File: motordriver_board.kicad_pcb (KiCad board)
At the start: 2 copper layers, 99.9 x 99.9 mm, 74 parts, among them IC1 AZ1117CH-3.3TRG1, J1 Conn_01x05_Socket, J10 RJ45, J11 USB_C_Receptacle_USB2.0, J12 Conn_01x03_Socket, J13 Conn_02x07_Odd_Even, J14 RJ45, J15 Conn_01x02_Socket, J2 Conn_01x02, J3 Conn_01x02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

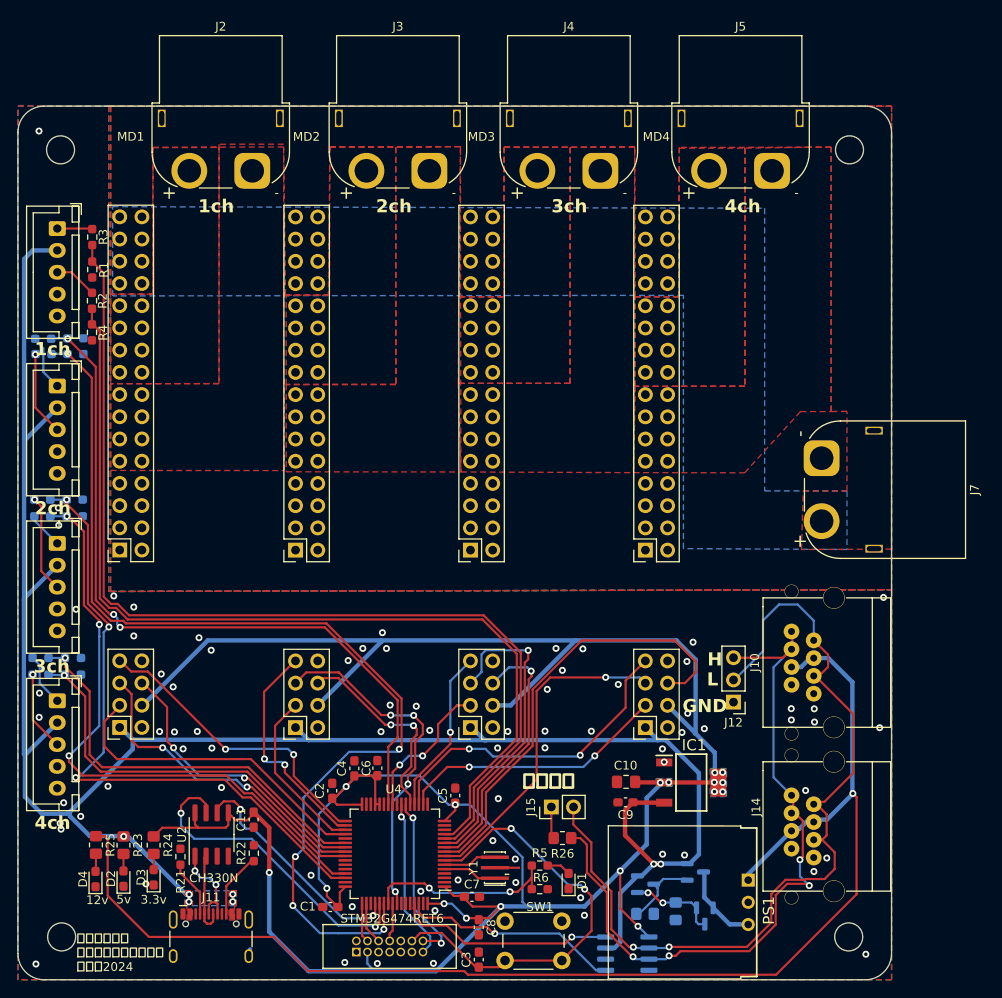
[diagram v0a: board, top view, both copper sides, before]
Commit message: 並列にXT60追加
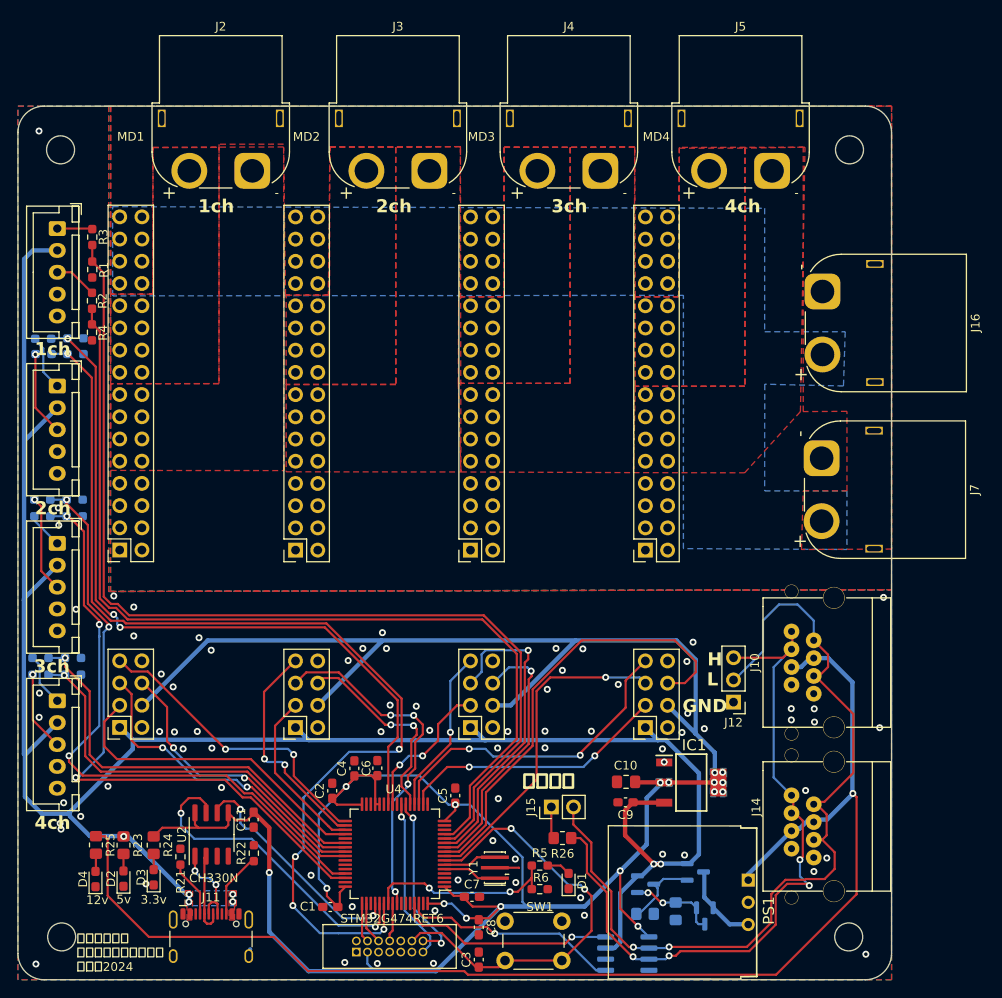
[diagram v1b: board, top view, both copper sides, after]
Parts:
- added J16: Conn_01x02, Connector_AMASS:AMASS_XT60PW-M_1x02_P7.20mm_Horizontal, F.Cu at (142.0, 61.2)
